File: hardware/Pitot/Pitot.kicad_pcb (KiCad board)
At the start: 2 copper layers, 52.2 x 61.5 mm, 62 parts, among them IC1 ABPMRRV060MG2A3, IC2 ABPMRRV060MG2A3, J1 53307-2471, J3 MX150_02x06_Vertical, J4 Conn_01x08, U2 LDO40LPURY

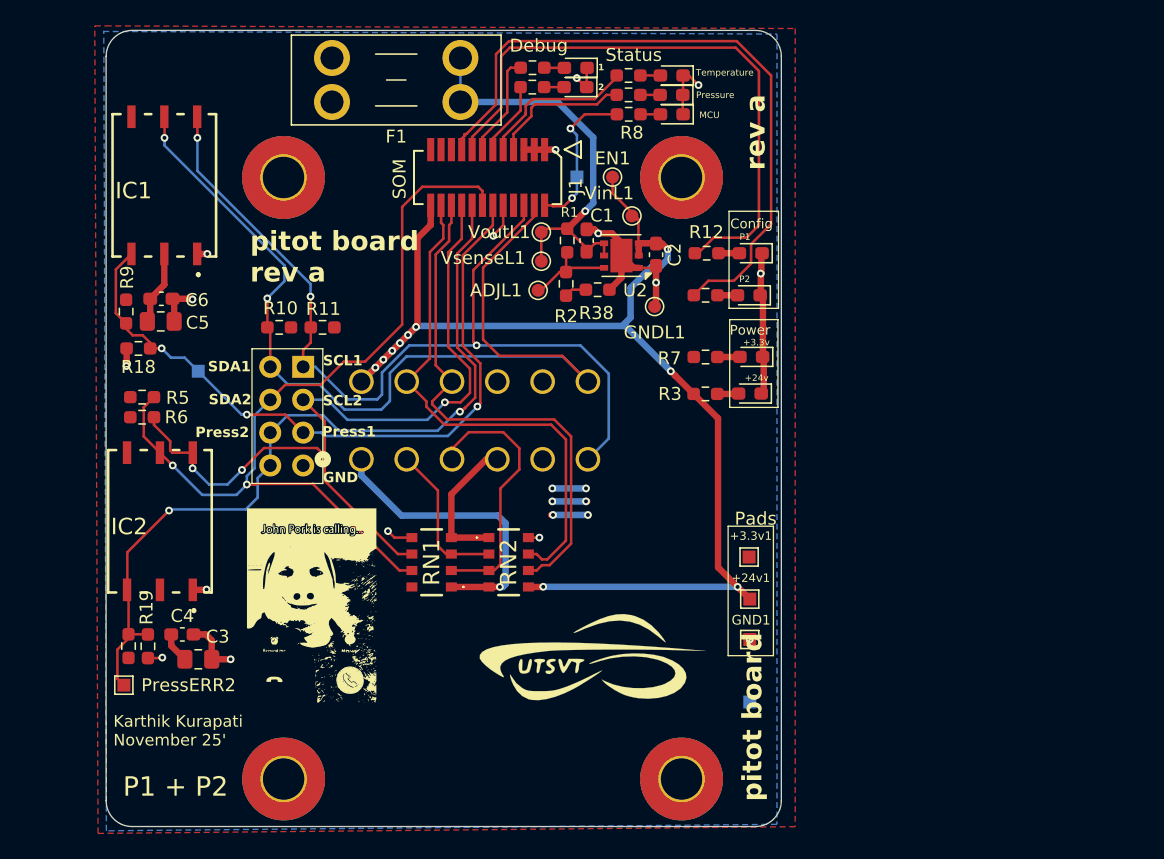
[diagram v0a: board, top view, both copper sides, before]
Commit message: Rev B Review (#2)
* schematic changes: ldo switched out of qfn, op amp footprint fixed, resistor array changed. need add correct stm changes

* finished sch + removed LDO

* removed LDO, added correct cube.

* op-amp changes

* layout finished, need to add some more silkscreen + ready for review!

* finished layout + silkscreen, ready to review.

* mac files removed

* made changes from review council

* added 3d models for 01x05 nanofits

* added stepfiles for sus-rh

* sus-rh production ready

* remove .DS_Store files

* fixed nanofit for linpot

* added "validated silkscreen"

* Added jlc assembly files

* pitot board sch review. the biggest change was the switch to nanofits and different pressure sensor

---------

Co-authored-by: Lakshay983 <56173382+Lakshay983@users.noreply.github.com>
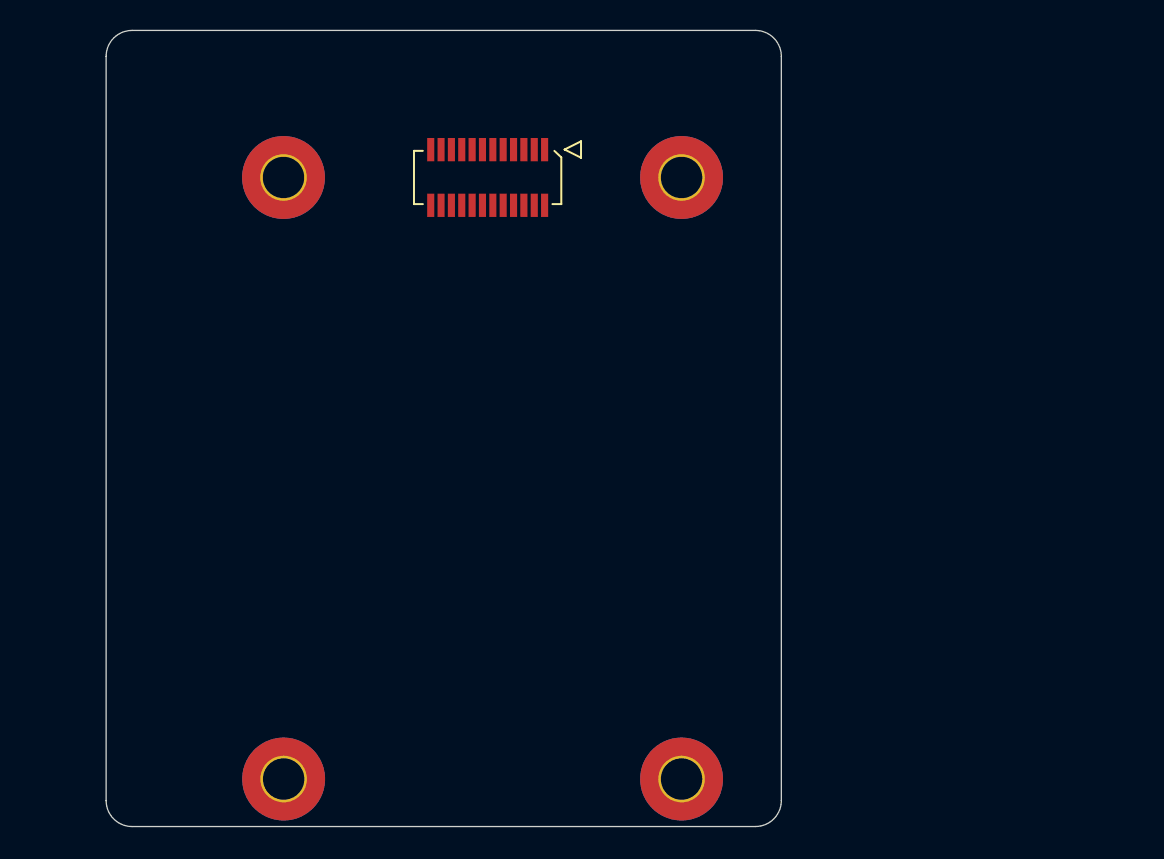
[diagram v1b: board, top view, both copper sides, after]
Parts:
- removed +24v1, +3.3MCU1, +3.3v1, GND1, GND2, PressERR1, PressERR2: TestPoint, TestPoint:TestPoint_Pad_1.0x1.0mm
- removed ADJL1: TP5, TestPoint:TestPoint_Pad_D1.0mm
- removed C1, C2: 1uF, Capacitor_SMD:C_0603_1608Metric_Pad1.08x0.95mm_HandSolder
- removed C3, C5: 10uf, Capacitor_SMD:C_0805_2012Metric_Pad1.18x1.45mm_HandSolder
- removed C4, C6: 0.1uF, Capacitor_SMD:C_0603_1608Metric_Pad1.08x0.95mm_HandSolder
- removed D1, D2, D3, D4, D5, D6, D7, D8, D9: LED, LED_SMD:LED_0603_1608Metric_Pad1.05x0.95mm_HandSolder
- removed EN1: TP2, TestPoint:TestPoint_Pad_D1.0mm
- removed F1: 500mA, Fuse:Fuseholder_Blade_Mini_Keystone_3568
- removed G***: LOGO, footprints:johnInverted
- removed G***: LOGO, UTSVT_Logos:UTSVT_Logo_Symbol
- removed G***: LHRs_LOGO, UTSVT_Logos:LHRs_LOGO
- removed G***: LOGO, footprints:diddybludInverted
- removed G***: LOGO, UTSVT_Logos:roosters
- removed GNDL1: TP6, TestPoint:TestPoint_Pad_D1.0mm
- removed IC1, IC2: ABPMRRV060MG2A3, footprints:ABPMRRV060MG2A3
- removed J3: MX150_02x06_Vertical, UTSVT_Connectors:MX150_02x06_Vertical
- removed J4: Conn_01x08, Connector_PinHeader_2.54mm:PinHeader_2x04_P2.54mm_Vertical
- removed R1: 10k, Resistor_SMD:R_0603_1608Metric_Pad0.98x0.95mm_HandSolder
- removed R10, R11, R18, R19, R3, R4, R5, R6, R9: 4.7k, Resistor_SMD:R_0603_1608Metric_Pad0.98x0.95mm_HandSolder
- removed R12, R13, R14, R15, R16, R17, R7, R8: 120, Resistor_SMD:R_0603_1608Metric_Pad0.98x0.95mm_HandSolder
- removed R2: 15k, Resistor_SMD:R_0603_1608Metric_Pad0.98x0.95mm_HandSolder
- removed R38: 2.49k, Resistor_SMD:R_0603_1608Metric_Pad0.98x0.95mm_HandSolder
- removed RN1, RN2: YC324-JK-070RL, 4pinRes:YC324JK07220RL
- removed U2: LDO40LPURY, Package_DFN_QFN:DFN-6-1EP_3x3mm_P0.95mm_EP1.7x2.6mm
- removed VinL1: TP1, TestPoint:TestPoint_Pad_D1.0mm
- removed VoutL1: TP3, TestPoint:TestPoint_Pad_D1.0mm
- removed VsenseL1: TP4, TestPoint:TestPoint_Pad_D1.0mm
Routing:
- net +24V: track 97.8 -> 0.00 mm, vias 10 -> 0
- net /SDA1: track 74.9 -> 0.00 mm, vias 2 -> 0
- net /SCL1: track 72.3 -> 0.00 mm, vias 3 -> 0
- net /SDA2: track 66.1 -> 0.00 mm, vias 2 -> 0
- net /SCL2: track 65.9 -> 0.00 mm, vias 3 -> 0
- net /pressERR_2: track 64.0 -> 0.00 mm, vias 2 -> 0
- net /pressERR_1: track 55.5 -> 0.00 mm, vias 3 -> 0
- net GND: track 52.8 -> 0.00 mm, vias 16 -> 0
- net /P2_LED: track 51.9 -> 0.00 mm
- net /P1_LED: track 46.8 -> 0.00 mm
- net /CAN_-: track 41.2 -> 0.00 mm
- net /CAN_+: track 40.7 -> 0.00 mm
- net Net-(U2-Vout): track 32.1 -> 0.00 mm, vias 1 -> 0
- net /Gen_1: track 22.9 -> 0.00 mm, vias 1 -> 0
- net /Gen_3: track 20.2 -> 0.00 mm
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- removed copper zone on F.Cu, net +3.3V
- removed copper zone on B.Cu, net GND
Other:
- board text removed: "+24v"
- board text removed: "+3.3v"
- board text removed: "1"
- board text removed: "2"
- board text removed: "Config"
- board text removed: "Debug"
- board text removed: "GND"
- board text removed: "Karthik Kurapati November 25'"
- board text removed: "MCU"
- board text removed: "P1"
- board text removed: "P1 + P2"
- board text removed: "P2"
- board text removed: "Pads"
- board text removed: "Power"
- board text removed: "Press1"
- board text removed: "Press2"
- board text removed: "Pressure"
- board text removed: "SCL1"
- board text removed: "SCL2"
- board text removed: "SDA1"
- board text removed: "SDA2"
- board text removed: "Status"
- board text removed: "Temperature"
- board text removed: "pitot board"
- board text removed: "pitot board rev a"
- board text removed: "rev a"

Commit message: added layout
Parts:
- added +24v1: TestPoint, TestPoint:TestPoint_Pad_1.0x1.0mm, F.Cu at (193.9, 72.2)
- added +3.3v1: TestPoint, TestPoint:TestPoint_Pad_1.0x1.0mm, F.Cu at (193.9, 75.2)
- added C1: 0.1uF, Capacitor_SMD:C_0603_1608Metric_Pad1.08x0.95mm_HandSolder, F.Cu at (120.2, 81.5)
- added C2: 0.1uF, Capacitor_SMD:C_0603_1608Metric_Pad1.08x0.95mm_HandSolder, F.Cu at (120.2, 103.8)
- added D1: LED, LED_SMD:LED_0603_1608Metric_Pad1.05x0.95mm_HandSolder, F.Cu at (167.4, 72.1)
- added D10: LED, LED_SMD:LED_0603_1608Metric_Pad1.05x0.95mm_HandSolder, F.Cu at (151.6, 52.7)
- added D2: LED, LED_SMD:LED_0603_1608Metric_Pad1.05x0.95mm_HandSolder, F.Cu at (167.4, 70.3)
- added D3: LED, LED_SMD:LED_0603_1608Metric_Pad1.05x0.95mm_HandSolder, F.Cu at (153.1, 52.7)
- added D4: LED, LED_SMD:LED_0603_1608Metric_Pad1.05x0.95mm_HandSolder, F.Cu at (143.1, 52.7)
- added D5: LED, LED_SMD:LED_0603_1608Metric_Pad1.05x0.95mm_HandSolder, F.Cu at (144.7, 52.7)
- added D8: LED, LED_SMD:LED_0603_1608Metric_Pad1.05x0.95mm_HandSolder, F.Cu at (148.6, 52.7)
- added D9: LED, LED_SMD:LED_0603_1608Metric_Pad1.05x0.95mm_HandSolder, F.Cu at (147.1, 52.7)
- added F1: 500mA, Fuse:Fuse_0603_1608Metric_Pad1.05x0.95mm_HandSolder, F.Cu at (156.8, 66.8)
- added F2: 500mA, Fuse:Fuse_0603_1608Metric_Pad1.05x0.95mm_HandSolder, F.Cu at (151.2, 99.5)
- added GND1: TestPoint, TestPoint:TestPoint_Pad_1.0x1.0mm, F.Cu at (193.9, 78.2)
- added GND2: TestPoint, TestPoint:TestPoint_Pad_1.0x1.0mm, F.Cu at (193.9, 81.3)
- added IC1: HSCDRRN010NDSA3, UTSVT_Connectors:HSCDRRN010NDSA3, F.Cu at (118.6, 79.0)
- added IC2: HSCDRRN010NDSA3, UTSVT_Connectors:HSCDRRN010NDSA3, F.Cu at (118.7, 101.0)
- added J2: Conn_01x05, Connector_Molex:Molex_Nano-Fit_105313-xx05_1x05_P2.50mm_Horizontal, B.Cu at (159.1, 89.5)
- added J3: Conn_01x04, Connector_Molex:Molex_Nano-Fit_105313-xx04_1x04_P2.50mm_Horizontal, B.Cu at (140.8, 101.2)
- added J4: Conn_01x08, Connector_PinHeader_2.54mm:PinHeader_2x04_P2.54mm_Vertical, F.Cu at (187.5, 72.9)
- added J5: Conn_01x05, Connector_Molex:Molex_Nano-Fit_105313-xx05_1x05_P2.50mm_Horizontal, B.Cu at (159.1, 104.0)
- added J6: Conn_01x04, Connector_Molex:Molex_Nano-Fit_105313-xx04_1x04_P2.50mm_Horizontal, B.Cu at (159.1, 75.0)
- added J7: Conn_01x04, Connector_PinHeader_2.54mm:PinHeader_1x04_P2.54mm_Vertical, F.Cu at (119.4, 57.2)
- added J8: Conn_01x02, Connector_PinHeader_2.54mm:PinHeader_1x02_P2.54mm_Vertical, F.Cu at (125.2, 106.7)
- added R1: 120, Resistor_SMD:R_0603_1608Metric_Pad0.98x0.95mm_HandSolder, F.Cu at (153.1, 56.1)
- added R12: 120, Resistor_SMD:R_0603_1608Metric_Pad0.98x0.95mm_HandSolder, F.Cu at (143.1, 56.0)
- added R13: 120, Resistor_SMD:R_0603_1608Metric_Pad0.98x0.95mm_HandSolder, F.Cu at (148.6, 56.1)
- added R14: 120, Resistor_SMD:R_0603_1608Metric_Pad0.98x0.95mm_HandSolder, F.Cu at (144.7, 56.0)
- added R15: 120, Resistor_SMD:R_0603_1608Metric_Pad0.98x0.95mm_HandSolder, F.Cu at (147.1, 56.1)
- added R2: 120, Resistor_SMD:R_0603_1608Metric_Pad0.98x0.95mm_HandSolder, F.Cu at (151.6, 56.1)
- added R3: 4.7k, Resistor_SMD:R_0603_1608Metric_Pad0.98x0.95mm_HandSolder, F.Cu at (164.0, 72.1)
- added R4: 0, Resistor_SMD:R_0603_1608Metric_Pad0.98x0.95mm_HandSolder, F.Cu at (162.8, 79.5)
- added R5: 0, Resistor_SMD:R_0603_1608Metric_Pad0.98x0.95mm_HandSolder, F.Cu at (155.8, 94.0)
- added R7: 120, Resistor_SMD:R_0603_1608Metric_Pad0.98x0.95mm_HandSolder, F.Cu at (164.0, 70.3)
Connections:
- J1 pad 12: /pressERR_1 -> unconnected-(J1-SPI2_NSS-Pad12)
- J1 pad 16: /pressERR_2 -> unconnected-(J1-SPI2_MOSI-Pad16)
- J1 pad 17: /P2_LED -> /Diff2
- J1 pad 19: unconnected-(J1-SPI1_NSS-Pad19) -> /Diff1
- J1 pad 2: +3.3VMCU -> +3.3V
- J1 pad 21: unconnected-(J1-SPI1_MISO-Pad21) -> /MISO
- J1 pad 23: unconnected-(J1-SPI1_SCK-Pad23) -> /SCLK
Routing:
- net +3.3V: track 0.00 -> 118.8 mm, vias 0 -> 2
- net +24V: track 0.00 -> 75.1 mm, vias 0 -> 1
- net /MISO: track 0.00 -> 54.2 mm
- net /CAN_+: track 0.00 -> 52.5 mm, vias 0 -> 1
- net /SCLK: track 0.00 -> 50.1 mm
- net /CAN_-: track 0.00 -> 49.5 mm
- net /SDA2: track 0.00 -> 47.0 mm
- net /Diff2: track 0.00 -> 38.4 mm
- net /SCL2: track 0.00 -> 37.6 mm, vias 0 -> 2
- net /Diff1: track 0.00 -> 22.7 mm
- net /SCL1: track 0.00 -> 21.6 mm
- net /P2_LED: track 0.00 -> 14.1 mm, vias 0 -> 2
- net unconnected-(J1-SPI2_NSS-Pad12): track 0.00 -> 13.7 mm
- net /SDA1: track 0.00 -> 13.5 mm
- net /P1_LED: track 0.00 -> 4.40 mm
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- added copper zone on B.Cu, net GND
- added copper zone on F.Cu, net GND

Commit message: ready to review
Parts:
- removed F2: 500mA, Fuse:Fuse_0603_1608Metric_Pad1.05x0.95mm_HandSolder
- removed J4: Conn_01x08, Connector_PinHeader_2.54mm:PinHeader_2x04_P2.54mm_Vertical
- removed J8: Conn_01x02, Connector_PinHeader_2.54mm:PinHeader_1x02_P2.54mm_Vertical
- added G***: LHRs_LOGO, UTSVT_Logos:LHRs_LOGO, F.Cu at (162.8, 52.8)
- added G***: LHRs_LOGO, UTSVT_Logos:LHRs_LOGO, B.Cu at (162.2, 52.8)
- added J10: Conn_01x03, Connector_PinHeader_2.54mm:PinHeader_1x03_P2.54mm_Vertical, F.Cu at (153.0, 109.0)
- added J9: LogicAnalyzer, UTSVT_Connectors:CONN_SFH11-xxxC-D05-ST-XX_SUL, F.Cu at (123.2, 52.7)
- added R10: 4.7k, Resistor_SMD:R_0603_1608Metric_Pad0.98x0.95mm_HandSolder, F.Cu at (145.8, 96.0)
- added R11: 4..7k, Resistor_SMD:R_0603_1608Metric_Pad0.98x0.95mm_HandSolder, F.Cu at (125.2, 63.5)
- added R16: 4.7k, Resistor_SMD:R_0603_1608Metric_Pad0.98x0.95mm_HandSolder, F.Cu at (129.8, 88.8)
- added R17: 4.7k, Resistor_SMD:R_0603_1608Metric_Pad0.98x0.95mm_HandSolder, F.Cu at (122.2, 105.8)
- added R18: 4.7k, Resistor_SMD:R_0603_1608Metric_Pad0.98x0.95mm_HandSolder, F.Cu at (126.2, 105.8)
- added R6: 4.7k, Resistor_SMD:R_0603_1608Metric_Pad0.98x0.95mm_HandSolder, F.Cu at (161.5, 69.8)
- added R8: 4.7k, Resistor_SMD:R_0603_1608Metric_Pad0.98x0.95mm_HandSolder, F.Cu at (154.1, 72.5)
- added R9: 4.7k, Resistor_SMD:R_0603_1608Metric_Pad0.98x0.95mm_HandSolder, F.Cu at (146.8, 97.5)
- +24v1, +3.3v1, GND1, GND2: footprint TestPoint:TestPoint_Pad_1.0x1.0mm -> TestPoint:TestPoint_THTPad_2.0x2.0mm_Drill1.0mm
- J7: value Conn_01x04 -> Conn_01x03; footprint Connector_PinHeader_2.54mm:PinHeader_1x04_P2.54mm_Vertical -> Connector_PinHeader_2.54mm:PinHeader_1x03_P2.54mm_Vertical
- moved GND1 75.2 mm to (120.4, 62.0)
- moved +24v1 39.1 mm to (167.3, 100.9)
- moved GND2 38.1 mm to (167.3, 108.6)
- moved +3.3v1 29.2 mm to (167.1, 63.8)
- moved J7 27.3 mm to (124.5, 84.0), turned to -90 degrees
- moved D4 2.89 mm to (140.2, 52.8)
- moved R12 2.89 mm to (140.2, 56.1)
- moved F1 2.70 mm to (154.1, 66.7), turned to 180 degrees
- moved D5 2.09 mm to (142.6, 52.7)
- moved R14 2.09 mm to (142.6, 56.1)
- moved R5 1.41 mm to (156.8, 93.0), turned to -90 degrees
- moved D3 1.41 mm to (154.5, 52.7)
- moved R1 1.41 mm to (154.5, 56.1)
- moved D9 0.85 mm to (146.3, 52.8)
- moved R15 0.85 mm to (146.3, 56.1)
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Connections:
- net /CAN_+ renamed /CAN_H
- net /CAN_- renamed /CAN_L
- F1 pad 1: Net-(J6-Pin_4) -> /fused_3.3v
- J1 pad 16: unconnected-(J1-SPI2_MOSI-Pad16) -> /P2_LED
- J3 pad 4: Net-(J3-Pin_4) -> /fused_3.3v
- J6 pad 4: Net-(J6-Pin_4) -> /fused_3.3v
- J7 pad 1: /MISO -> /SCLK
- J7 pad 2: /SCLK -> /MISO
- J7 pad 3: /Diff1 -> GND
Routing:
- net /fused_3.3v: track 0.00 -> 42.0 mm, vias 0 -> 4
- net /SDA2: track 47.0 -> 82.8 mm, vias 0 -> 1
- net /SCL2: track 37.6 -> 72.6 mm, vias 2 -> 3
- net +3.3V: track 118.8 -> 149.4 mm, vias 2 -> 8
- net /SDA1: track 13.5 -> 43.7 mm, vias 0 -> 2
- net /SCLK: track 50.1 -> 74.7 mm, vias 0 -> 4
- net /MISO: track 54.2 -> 76.8 mm, vias 0 -> 4
- net /SCL1: track 21.6 -> 42.1 mm, vias 0 -> 2
- net +24V: track 75.1 -> 90.5 mm, vias 1 -> 0
- net unconnected-(J1-SPI2_NSS-Pad12): track 13.7 -> 0.00 mm
- net /Diff1: track 22.7 -> 33.3 mm
- net GND: track 2.93 -> 13.0 mm, vias 0 -> 167
- net /diff_stat: track 1.10 -> 7.23 mm
- net /temp_stat: track 0.91 -> 5.77 mm
- net /P1_LED: track 4.40 -> 8.43 mm
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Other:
- board text added: "+24v"
- board text added: "+3.3v"
- board text added: "3.3v"
- board text added: "CAN_H"
- board text added: "CAN_L"
- board text added: "Configuration"
- board text added: "D1"
- board text added: "D2"
- board text added: "Debug"
- board text added: "February 2026"
- board text added: "GND"
- board text added: "Karthik Kurapati"
- board text added: "MISO"
- board text added: "P1"
- board text added: "P2"
- board text added: "Power"
- board text added: "Pressure"
- board text added: "SCL1"
- board text added: "SCL2"
- board text added: "SCLK"
- board text added: "SDA1"
- board text added: "SDA2"
- board text added: "SHIELD"
- board text added: "Status"
- board text added: "Temp"

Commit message: finished pitot board
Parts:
- removed J10, J7: Conn_01x03, Connector_PinHeader_2.54mm:PinHeader_1x03_P2.54mm_Vertical
- added G***: LOGO, footprints:whoishe, F.Cu at (133.8, 99.2)
- added G***: LOGO, footprints:plane10, F.Cu at (135.5, 73.2)
- added G***: LOGO, footprints:golem_inverted, F.Cu at (146.8, 73.0)
- added G***: LOGO, footprints:ravishah, F.Cu at (142.2, 87.2)
- added G***: LOGO, footprints:plane10, B.Cu at (141.8, 83.8)
- R10, R16, R6, R8, R9: value 4.7k -> 10k
- R11: value 4..7k -> 10k
- moved GND1 1.28 mm to (120.4, 60.8)
- moved C1 0.70 mm to (120.2, 82.2)
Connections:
- J9 pad 3: unconnected-(J9-CH7-Pad3) -> /Diff2
- J9 pad 4: unconnected-(J9-CH6-Pad4) -> /Diff1
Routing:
- net /Diff2: track 41.4 -> 64.8 mm, vias 0 -> 1
- net /SDA2: track 82.8 -> 69.9 mm
- net /SCL2: track 72.6 -> 62.1 mm
- net /Diff1: track 33.3 -> 42.3 mm
- net GND: track 13.0 -> 8.92 mm, vias 167 -> 109
- net /MISO: track 76.8 -> 75.5 mm
- net /SCLK: track 74.7 -> 74.2 mm
- net +3.3V: track 149.4 -> 149.9 mm
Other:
- board text added: "CAN INPUT"
- board text added: "CAN Output"
- board text added: "P1 + P2"
- board text added: "Temperature 1"
- board text added: "Temperature 2"
- board text added: "pitot board"
- board text added: "rev B"
